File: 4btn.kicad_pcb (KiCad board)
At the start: 2 copper layers, 42.5 x 26.3 mm, 38 parts, among them CON1 AVR-ISP, IC1 ATTINY88-A, Q1 2N7002, Q2 2N7002, U1 74HC14D_653, U2 SW_SPST, U3 SW_SPST, U6 SW_SPST, U7 SW_SPST, U8 SCL SCA GND Vcc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

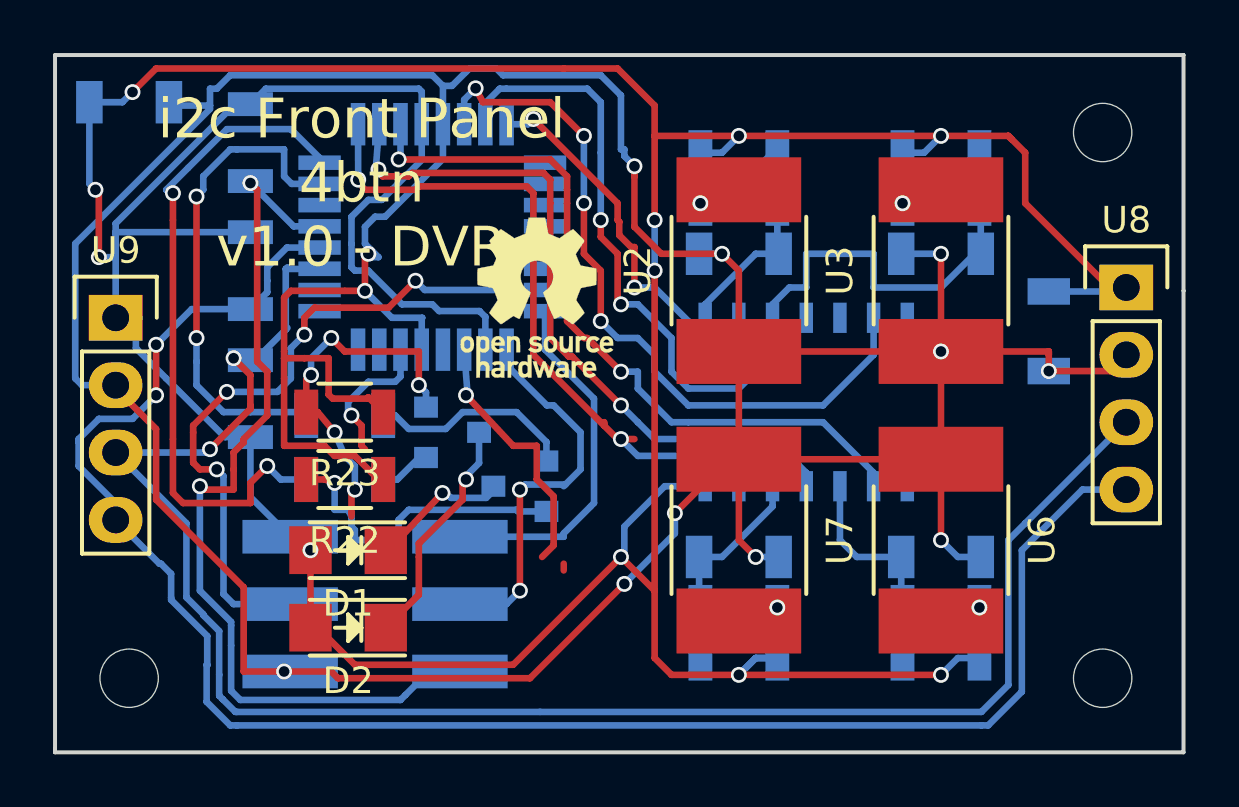
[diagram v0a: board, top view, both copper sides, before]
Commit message: Headers aligned better
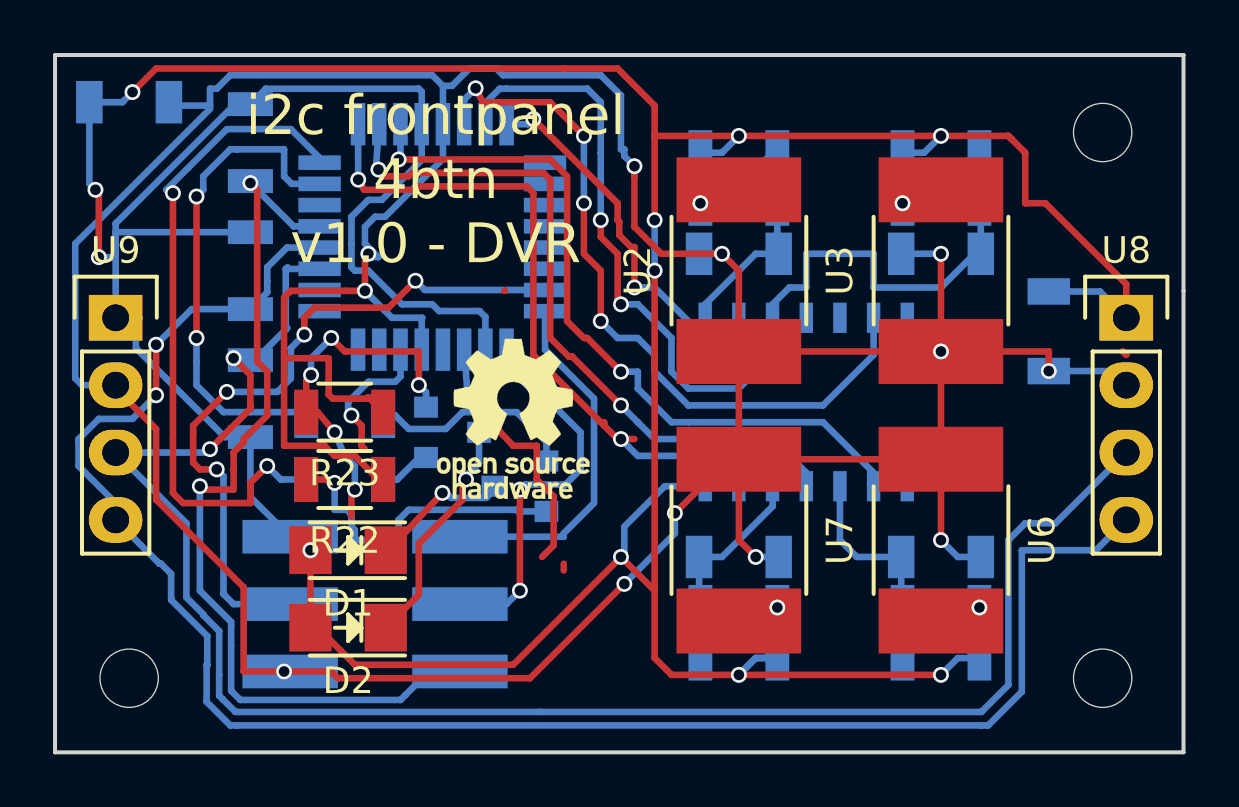
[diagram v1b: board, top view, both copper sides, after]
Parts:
- moved REF*** 4.66 mm to (50.0, 34.8)
- moved U8 1.14 mm to (73.2, 31.0)
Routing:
- net VCC: track 168.3 -> 169.9 mm
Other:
- board text added: "i2c frontpanel 4btn v1.0 - DVR"
- board text removed: "i2c Front Panel 4btn v1.0 - DVR"
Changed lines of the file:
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@@
     (links 74)
     (no_connects 0)
-    (area 32.690999 21.006999 124.662001 47.825)
+    (area 32.690999 21.006999 75.386001 47.446001)
     (thickness 1.6)
     (drawings 12)
-    (tracks 655)
+    (tracks 657)
     (zones 0)
     (modules 38)
@@
   )
   (module Pin_Headers:Pin_Header_Straight_1x04 (layer F.Cu)
-    (at 73.152 29.845)
+    (at 73.152 30.988)
     (descr "Through hole pin header")
     (tags "pin header")
@@
   )
   (module Symbols:OSHW-Logo_5.7x6mm_SilkScreen (layer F.Cu)
-    (at 50.927 30.226)
+    (at 50.038 34.798)
     (descr "Open Source Hardware Logo")
     (tags "Logo OSHW")
@@
     (effects (font (size 1 1) (thickness 0.2)) (justify mirror))
   )
-  (gr_text "i2c Front Panel\n4btn\nv1.0 - DVR" (at 44.323 25.908) (layer F.SilkS)
+  (gr_text "i2c frontpanel\n4btn\nv1.0 - DVR" (at 47.117 25.781) (layer F.SilkS)
     (effects (font (size 1.5 1.5) (thickness 0.3)))
   )
@@
   (segment (start 49.714998 29.969249) (end 49.714998 29.969249) (width 0.25) (layer F.Cu) (net 0))
   (segment (start 49.714998 29.969249) (end 49.717749 29.972) (width 0.25) (layer F.Cu) (net 0))
+  (segment (start 73.025 32.258) (end 73.152 32.385) (width 0.25) (layer F.Cu) (net 0))
+  (segment (start 73.025 32.258) (end 73.152 32.385) (width 0.25) (layer F.Cu) (net 0))
+  (segment (start 70.231 29.996) (end 72.16 29.996) (width 0.25) (layer B.Cu) (net 1))
+  (segment (start 72.16 29.996) (end 73.152 30.988) (width 0.25) (layer B.Cu) (net 1))
+  (segment (start 69.342 26.67) (end 70.104 26.67) (width 0.25) (layer F.Cu) (net 1))
+  (segment (start 68.834 24.257) (end 69.342 24.765) (width 0.25) (layer F.Cu) (net 1))
+  (segment (start 69.342 26.67) (end 69.342 24.765) (width 0.25) (layer F.Cu) (net 1))
+  (segment (start 73.152 29.718) (end 73.152 30.988) (width 0.25) (layer F.Cu) (net 1))
+  (segment (start 70.104 26.67) (end 73.152 29.718) (width 0.25) (layer F.Cu) (net 1))
   (segment (start 66.167 24.13) (end 68.707 24.13) (width 0.25) (layer F.Cu) (net 1))
   (segment (start 68.707 24.13) (end 68.834 24.257) (width 0.25) (layer F.Cu) (net 1))
@@
   (segment (start 57.277 37.338) (end 55.753 37.338) (width 0.25) (layer B.Cu) (net 1))
   (segment (start 54.229 39.878) (end 54.102 40.005) (width 0.25) (layer B.Cu) (net 1))
-  (segment (start 70.231 29.996) (end 73.001 29.996) (width 0.25) (layer B.Cu) (net 1))
-  (segment (start 73.001 29.996) (end 73.152 29.845) (width 0.25) (layer B.Cu) (net 1))
   (segment (start 34.06 22.86) (end 34.06 25.932) (width 0.25) (layer B.Cu) (net 1))
   (segment (start 34.417 28.702) (end 35.052 28.702) (width 0.25) (layer B.Cu) (net 1))
@@
   (segment (start 35.052 30.988) (end 35.052 28.702) (width 0.25) (layer B.Cu) (net 1))
   (segment (start 35.052 28.702) (end 35.052 28.194) (width 0.25) (layer B.Cu) (net 1))
-  (segment (start 73.152 29.845) (end 72.517 29.845) (width 0.25) (layer F.Cu) (net 1))
-  (segment (start 72.517 29.845) (end 69.342 26.67) (width 0.25) (layer F.Cu) (net 1))
-  (segment (start 69.342 26.67) (end 69.342 24.765) (width 0.25) (layer F.Cu) (net 1))
-  (segment (start 69.342 24.765) (end 68.834 24.257) (width 0.25) (layer F.Cu) (net 1))
   (segment (start 68.834 24.257) (end 68.707 24.13) (width 0.25) (layer F.Cu) (net 1))
   (segment (start 58.547 24.13) (end 55.372 24.13) (width 0.25) (layer F.Cu) (net 1))
@@
   (via (at 58.547 24.13) (size 0.6) (drill 0.4) (layers F.Cu B.Cu) (net 1))
   (segment (start 57.912 24.765) (end 58.547 24.13) (width 0.25) (layer B.Cu) (net 1))
+  (segment (start 70.231 32.996) (end 72.62 32.996) (width 0.25) (layer B.Cu) (net 2))
+  (segment (start 72.62 32.996) (end 73.152 33.528) (width 0.25) (layer B.Cu) (net 2))
   (segment (start 66.167 32.258) (end 66.167 28.575) (width 0.25) (layer F.Cu) (net 2))
   (segment (start 66.167 28.575) (end 64.667 28.575) (width 0.25) (layer B.Cu) (net 2))
@@
   (segment (start 41.402 44.323) (end 41.631 44.323) (width 0.25) (layer B.Cu) (net 2))
   (segment (start 35.052 33.528) (end 35.052 33.655) (width 0.25) (layer F.Cu) (net 2))
-  (segment (start 72.541 32.996) (end 70.231 32.996) (width 0.25) (layer F.Cu) (net 2))
   (segment (start 70.231 32.258) (end 70.231 32.996) (width 0.25) (layer F.Cu) (net 2))
   (segment (start 70.231 32.258) (end 70.231 32.385) (width 0.25) (layer F.Cu) (net 2))
   (via (at 70.231 32.996) (size 0.6) (drill 0.4) (layers F.Cu B.Cu) (net 2))
-  (segment (start 72.541 32.996) (end 73.152 32.385) (width 0.25) (layer F.Cu) (net 2))
-  (segment (start 73.025 32.258) (end 73.152 32.385) (width 0.25) (layer F.Cu) (net 2))
   (via (at 66.167 32.258) (size 0.6) (drill 0.4) (layers F.Cu B.Cu) (net 2))
   (segment (start 66.167 32.258) (end 64.897 30.988) (width 0.25) (layer B.Cu) (net 2))
@@
   (segment (start 33.528 33.274) (end 33.528 28.194) (width 0.25) (layer B.Cu) (net 2))
   (segment (start 47.39 22.244) (end 47.39 23.69) (width 0.25) (layer B.Cu) (net 2))
-  (segment (start 73.025 32.258) (end 73.152 32.385) (width 0.25) (layer F.Cu) (net 2))
   (segment (start 57.785 36.322) (end 58.547 36.322) (width 0.25) (layer F.Cu) (net 2))
   (segment (start 58.547 36.322) (end 66.167 36.322) (width 0.25) (layer F.Cu) (net 2))
@@
   (segment (start 43.815 34.163) (end 43.815 34.544) (width 0.25) (layer B.Cu) (net 29))
   (segment (start 44.323 35.814) (end 44.45 35.941) (width 0.25) (layer F.Cu) (net 29))
+  (segment (start 69.342 38.735) (end 70.485 38.735) (width 0.25) (layer B.Cu) (net 34))
   (segment (start 51.054 45.847) (end 67.691 45.847) (width 0.25) (layer B.Cu) (net 34))
   (segment (start 69.342 38.735) (end 68.707 39.37) (width 0.25) (layer B.Cu) (net 34))
@@
   (segment (start 38.954499 44.45) (end 38.954499 45.236895) (width 0.25) (layer B.Cu) (net 34))
   (segment (start 39.564604 45.847) (end 39.624 45.847) (width 0.25) (layer B.Cu) (net 34))
-  (segment (start 69.342 38.735) (end 73.152 34.925) (width 0.25) (layer B.Cu) (net 34))
+  (segment (start 70.485 38.735) (end 73.152 36.068) (width 0.25) (layer B.Cu) (net 34))
   (segment (start 40.132 34.417) (end 40.132 33.147) (width 0.25) (layer F.Cu) (net 34))
   (segment (start 39.497 32.512) (end 39.571 32.586) (width 0.25) (layer B.Cu) (net 34))
@@
   (segment (start 40.312 32.586) (end 41.4655 31.4325) (width 0.25) (layer B.Cu) (net 34))
   (segment (start 41.4655 31.4325) (end 41.529 31.369) (width 0.25) (layer B.Cu) (net 34))
+  (segment (start 69.215 39.751) (end 72.009 39.751) (width 0.25) (layer B.Cu) (net 35))
+  (segment (start 35.052 38.608) (end 36.703 40.259) (width 0.25) (layer B.Cu) (net 35))
+  (segment (start 36.703 40.259) (end 36.760998 40.259) (width 0.25) (layer B.Cu) (net 35))
+  (segment (start 36.760998 40.259) (end 37.141998 40.64) (width 0.25) (layer B.Cu) (net 35))
+  (segment (start 37.141998 40.64) (end 37.141998 41.529) (width 0.25) (layer B.Cu) (net 35))
+  (segment (start 38.481 44.069) (end 38.504497 44.092497) (width 0.25) (layer B.Cu) (net 35))
+  (segment (start 38.481 45.466) (end 38.481 44.069) (width 0.25) (layer B.Cu) (net 35))
+  (segment (start 39.37 46.355) (end 38.481 45.466) (width 0.25) (layer B.Cu) (net 35))
+  (segment (start 39.624 46.355) (end 39.37 46.355) (width 0.25) (layer B.Cu) (net 35))
+  (segment (start 37.141998 41.622897) (end 38.504497 42.985396) (width 0.25) (layer B.Cu) (net 35))
+  (segment (start 38.504497 42.985396) (end 38.504497 44.069) (width 0.25) (layer B.Cu) (net 35))
+  (segment (start 38.504497 44.069) (end 38.504497 44.092497) (width 0.25) (layer B.Cu) (net 35))
+  (segment (start 37.141998 41.529) (end 37.141998 41.622897) (width 0.25) (layer B.Cu) (net 35))
+  (segment (start 67.945 46.355) (end 69.215 45.085) (width 0.25) (layer B.Cu) (net 35))
+  (segment (start 69.215 45.085) (end 69.215 39.751) (width 0.25) (layer B.Cu) (net 35))
+  (segment (start 67.691 46.355) (end 67.945 46.355) (width 0.25) (layer B.Cu) (net 35))
   (segment (start 67.691 46.355) (end 39.624 46.355) (width 0.25) (layer B.Cu) (net 35))
-  (segment (start 67.691 46.355) (end 67.945 46.355) (width 0.25) (layer B.Cu) (net 35))
-  (segment (start 73.152 37.465) (end 71.501 37.465) (width 0.25) (layer B.Cu) (net 35))
-  (segment (start 69.215 39.751) (end 71.501 37.465) (width 0.25) (layer B.Cu) (net 35))
-  (segment (start 69.215 45.085) (end 69.215 39.751) (width 0.25) (layer B.Cu) (net 35))
-  (segment (start 67.945 46.355) (end 69.215 45.085) (width 0.25) (layer B.Cu) (net 35))
-  (segment (start 37.141998 41.529) (end 37.141998 41.622897) (width 0.25) (layer B.Cu) (net 35))
-  (segment (start 38.504497 44.069) (end 38.504497 44.092497) (width 0.25) (layer B.Cu) (net 35))
-  (segment (start 38.504497 42.985396) (end 38.504497 44.069) (width 0.25) (layer B.Cu) (net 35))
-  (segment (start 37.141998 41.622897) (end 38.504497 42.985396) (width 0.25) (layer B.Cu) (net 35))
-  (segment (start 39.624 46.355) (end 39.37 46.355) (width 0.25) (layer B.Cu) (net 35))
-  (segment (start 39.37 46.355) (end 38.481 45.466) (width 0.25) (layer B.Cu) (net 35))
-  (segment (start 38.481 45.466) (end 38.481 44.069) (width 0.25) (layer B.Cu) (net 35))
-  (segment (start 38.481 44.069) (end 38.504497 44.092497) (width 0.25) (layer B.Cu) (net 35))
-  (segment (start 37.141998 40.64) (end 37.141998 41.529) (width 0.25) (layer B.Cu) (net 35))
-  (segment (start 36.760998 40.259) (end 37.141998 40.64) (width 0.25) (layer B.Cu) (net 35))
-  (segment (start 36.703 40.259) (end 36.760998 40.259) (width 0.25) (layer B.Cu) (net 35))
-  (segment (start 36.703 40.259) (end 35.052 38.608) (width 0.25) (layer B.Cu) (net 35))
+  (segment (start 72.009 39.751) (end 73.152 38.608) (width 0.25) (layer B.Cu) (net 35))
   (segment (start 33.655 35.687) (end 33.655 35.56) (width 0.25) (layer B.Cu) (net 35))
   (segment (start 33.655 35.56) (end 34.417 34.798) (width 0.25) (layer B.Cu) (net 35))
